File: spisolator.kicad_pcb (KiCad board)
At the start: 2 copper layers, 12 parts, among them J1 Conn_01x03_Male, J2 Conn_01x03_Male, P1 CONN_02X04, P2 CONN_02X04, U1 4066, U2 25LXX, U3 4066

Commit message: pcb: reduced the board
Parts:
- moved C2 13.2 mm to (151.8, 86.4)
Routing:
- net /CLK_FL: track 20.3 -> 16.1 mm, vias 0 -> 2
- net /SO_FL: track 17.3 -> 14.5 mm, vias 0 -> 2
- net +3V3: track 51.8 -> 50.0 mm
- net /SI_FL: track 26.2 -> 27.3 mm
- net /CLK_MB: track 24.3 -> 25.5 mm
- net /SI_MB: track 18.9 -> 19.4 mm, vias 0 -> 2
- added copper zone on F.Cu, net GND
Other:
- board outline added: 71.8 x 34.8 mm

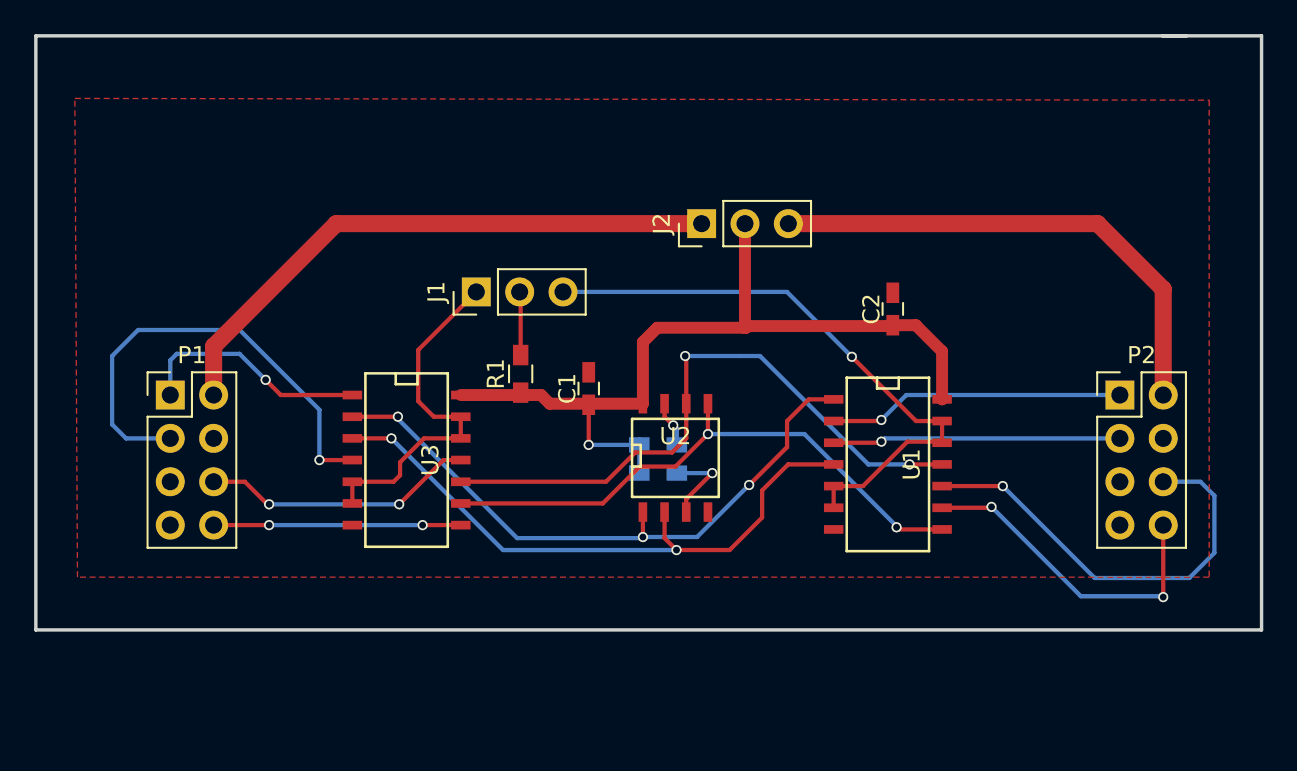
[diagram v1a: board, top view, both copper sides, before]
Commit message: pcb: started over the wiring
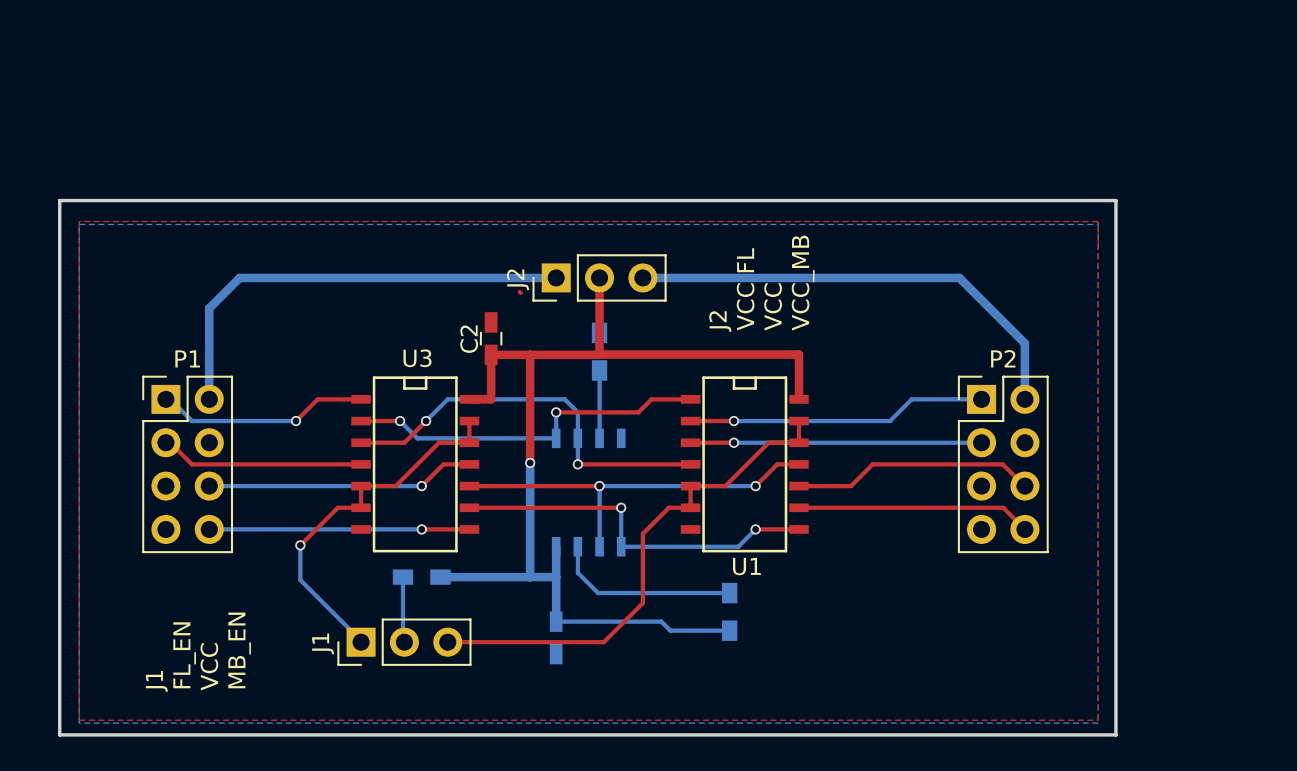
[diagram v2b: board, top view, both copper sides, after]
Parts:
- C1, R1, U2: moved to B.Cu
- moved C2 23.6 mm to (128.3, 88.1)
- moved J1 21.6 mm to (120.7, 105.9)
- moved C1 14.7 mm to (132.1, 105.7), turned to 270 degrees
- moved R1 13.2 mm to (124.2, 102.1), turned to 180 degrees
- moved R3 10.6 mm to (142.2, 104.1), turned to 90 degrees
- moved J2 9.09 mm to (132.1, 84.6)
- moved U1 8.38 mm to (143.3, 95.5)
- moved P2 8.10 mm to (157.0, 91.7)
- moved R2 7.90 mm to (134.6, 88.9), turned to 90 degrees
- moved U2 5.47 mm to (134.0, 97.2)
- moved U3 0.57 mm to (124.0, 95.5)
- moved P1 0.36 mm to (109.2, 91.7)
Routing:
- net +3V3: track 50.0 -> 66.8 mm
- net /~CS: track 37.0 -> 21.6 mm, vias 3 -> 2
- net /SI_FL: track 27.3 -> 12.0 mm, vias 1 -> 0
- net /CLK: track 36.8 -> 23.4 mm
- net /SO: track 36.4 -> 23.7 mm
- net /SI: track 34.0 -> 22.0 mm
- net /CLK_MB: track 25.5 -> 14.3 mm, vias 1 -> 0
- net Net-(R3-Pad2): track 2.71 -> 10.9 mm, vias 1 -> 0
- net VCC_Flasher: track 34.4 -> 26.4 mm
- net /SI_MB: track 19.4 -> 13.8 mm, vias 2 -> 0
- net /EN_MB: track 35.3 -> 29.8 mm, vias 1 -> 0
- net VCC_Mainboard: track 29.8 -> 27.2 mm
- net /~CS_FL: track 13.9 -> 12.5 mm
- net /~WP: track 4.99 -> 4.04 mm, vias 1 -> 0
- net /SO_FL: track 14.5 -> 15.2 mm, vias 2 -> 1
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- added copper zone on B.Cu, net GND
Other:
- board size 71.8 x 34.8 mm -> 61.9 x 31.3 mm
- board text added: "J1 FL_EN VCC MB_EN"
- board text added: "J2 VCC FL VCC VCC_MB"
- board text added: "spisolator2 version 0.2 https://github.com/lynxis/spisolator2"

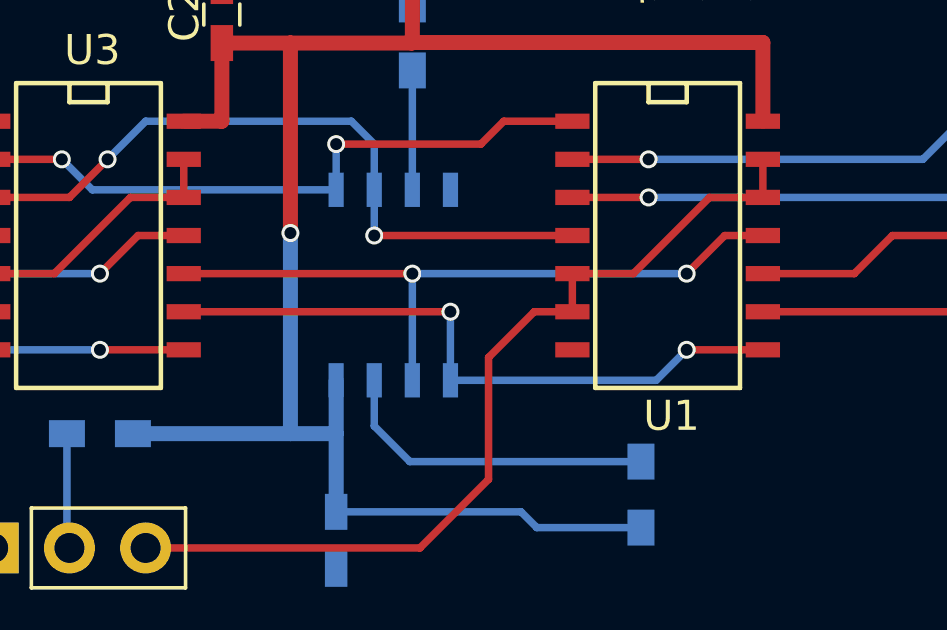
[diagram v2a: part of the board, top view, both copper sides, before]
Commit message: pcb: remove some 90o corners
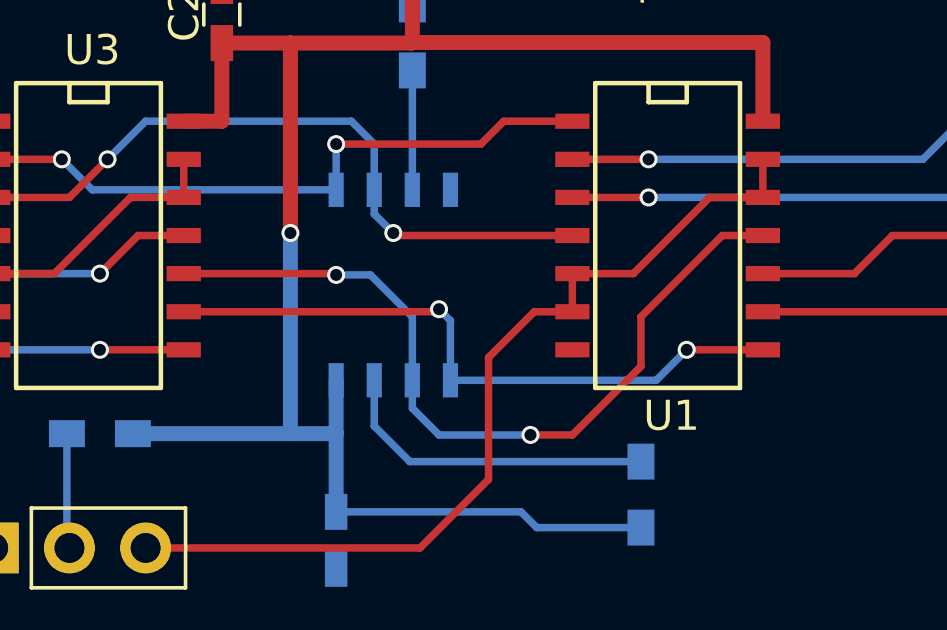
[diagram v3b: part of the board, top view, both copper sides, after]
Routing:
- net /CLK: track 23.4 -> 27.0 mm
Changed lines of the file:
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@@
     (thickness 1.6)
     (drawings 7)
-    (tracks 118)
+    (tracks 130)
     (zones 0)
     (modules 12)
@@
     (34 B.Paste user)
     (35 F.Paste user)
-    (36 B.SilkS user)
+    (36 B.SilkS user hide)
     (37 F.SilkS user)
     (38 B.Mask user)
@@
   )
   (setup
-    (last_trace_width 0.5)
+    (last_trace_width 0.25)
     (user_trace_width 0.5)
     (trace_clearance 0.2)
@@
   (segment (start 122.936 92.964) (end 123.952 93.98) (width 0.25) (layer B.Cu) (net 22))
   (via (at 122.936 92.964) (size 0.6) (drill 0.4) (layers F.Cu B.Cu) (net 22))
-  (segment (start 133.35 93.98) (end 133.35 95.504) (width 0.25) (layer B.Cu) (net 23))
-  (segment (start 133.35 95.504) (end 139.954 95.504) (width 0.25) (layer F.Cu) (net 23))
-  (via (at 133.35 95.504) (size 0.6) (drill 0.4) (layers F.Cu B.Cu) (net 23))
+  (segment (start 133.35 93.98) (end 133.35 94.785) (width 0.25) (layer B.Cu) (net 23) (status 400000))
+  (segment (start 134.069 95.504) (end 139.954 95.504) (width 0.25) (layer F.Cu) (net 23) (status 800000))
+  (segment (start 133.985 95.42) (end 134.069 95.504) (width 0.25) (layer F.Cu) (net 23))
+  (via (at 133.985 95.42) (size 0.6) (drill 0.4) (layers F.Cu B.Cu) (net 23))
+  (segment (start 133.35 94.785) (end 133.985 95.42) (width 0.25) (layer B.Cu) (net 23))
   (segment (start 120.65 94.234) (end 123.19 94.234) (width 0.25) (layer F.Cu) (net 23))
   (segment (start 133.35 92.456) (end 133.35 93.98) (width 0.25) (layer B.Cu) (net 23))
@@
   (via (at 124.46 92.964) (size 0.6) (drill 0.4) (layers F.Cu B.Cu) (net 23))
   (segment (start 123.19 94.234) (end 124.46 92.964) (width 0.25) (layer F.Cu) (net 23))
-  (segment (start 135.89 100.33) (end 135.89 98.044) (width 0.25) (layer B.Cu) (net 24))
-  (segment (start 135.89 98.044) (end 127 98.044) (width 0.25) (layer F.Cu) (net 24))
-  (via (at 135.89 98.044) (size 0.6) (drill 0.4) (layers F.Cu B.Cu) (net 24))
+  (segment (start 127 98.044) (end 135.425 98.044) (width 0.25) (layer F.Cu) (net 24) (status 400000))
+  (segment (start 135.89 98.341) (end 135.89 100.33) (width 0.25) (layer B.Cu) (net 24) (status 800000))
+  (segment (start 135.509 97.96) (end 135.89 98.341) (width 0.25) (layer B.Cu) (net 24))
+  (via (at 135.509 97.96) (size 0.6) (drill 0.4) (layers F.Cu B.Cu) (net 24))
+  (segment (start 135.425 98.044) (end 135.509 97.96) (width 0.25) (layer F.Cu) (net 24))
   (segment (start 135.89 100.33) (end 142.748 100.33) (width 0.25) (layer B.Cu) (net 24))
   (segment (start 143.764 99.314) (end 146.304 99.314) (width 0.25) (layer F.Cu) (net 24))
   (via (at 143.764 99.314) (size 0.6) (drill 0.4) (layers F.Cu B.Cu) (net 24))
   (segment (start 142.748 100.33) (end 143.764 99.314) (width 0.25) (layer B.Cu) (net 24))
-  (segment (start 134.62 96.774) (end 143.764 96.774) (width 0.25) (layer B.Cu) (net 25))
-  (via (at 143.764 96.774) (size 0.6) (drill 0.4) (layers F.Cu B.Cu) (net 25))
-  (segment (start 143.764 96.774) (end 145.034 95.504) (width 0.25) (layer F.Cu) (net 25))
-  (segment (start 145.034 95.504) (end 146.304 95.504) (width 0.25) (layer F.Cu) (net 25))
-  (segment (start 134.62 100.33) (end 134.62 96.774) (width 0.25) (layer B.Cu) (net 25))
-  (segment (start 134.62 96.774) (end 127 96.774) (width 0.25) (layer F.Cu) (net 25))
-  (via (at 134.62 96.774) (size 0.6) (drill 0.4) (layers F.Cu B.Cu) (net 25))
+  (segment (start 127 96.774) (end 132.037 96.774) (width 0.25) (layer F.Cu) (net 25) (status 400000))
+  (segment (start 134.62 98.214) (end 134.62 100.33) (width 0.25) (layer B.Cu) (net 25) (status 800000))
+  (segment (start 133.223 96.817) (end 134.62 98.214) (width 0.25) (layer B.Cu) (net 25))
+  (segment (start 132.08 96.817) (end 133.223 96.817) (width 0.25) (layer B.Cu) (net 25))
+  (via (at 132.08 96.817) (size 0.6) (drill 0.4) (layers F.Cu B.Cu) (net 25))
+  (segment (start 132.037 96.774) (end 132.08 96.817) (width 0.25) (layer F.Cu) (net 25))
+  (segment (start 146.304 95.504) (end 144.95 95.504) (width 0.25) (layer F.Cu) (net 25) (status 400000))
+  (segment (start 134.62 101.262) (end 134.62 100.33) (width 0.25) (layer B.Cu) (net 25) (status 800000))
+  (segment (start 135.509 102.151) (end 134.62 101.262) (width 0.25) (layer B.Cu) (net 25))
+  (segment (start 138.557 102.151) (end 135.509 102.151) (width 0.25) (layer B.Cu) (net 25))
+  (via (at 138.557 102.151) (size 0.6) (drill 0.4) (layers F.Cu B.Cu) (net 25))
+  (segment (start 139.954 102.151) (end 138.557 102.151) (width 0.25) (layer F.Cu) (net 25))
+  (segment (start 142.24 99.865) (end 139.954 102.151) (width 0.25) (layer F.Cu) (net 25))
+  (segment (start 142.24 98.214) (end 142.24 99.865) (width 0.25) (layer F.Cu) (net 25))
+  (segment (start 144.95 95.504) (end 142.24 98.214) (width 0.25) (layer F.Cu) (net 25))
   (zone (net 2) (net_name GND) (layer F.Cu) (hatch edge 0.508)
     (connect_pads (clearance 0.508))
